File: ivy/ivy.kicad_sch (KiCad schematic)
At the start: 0 parts

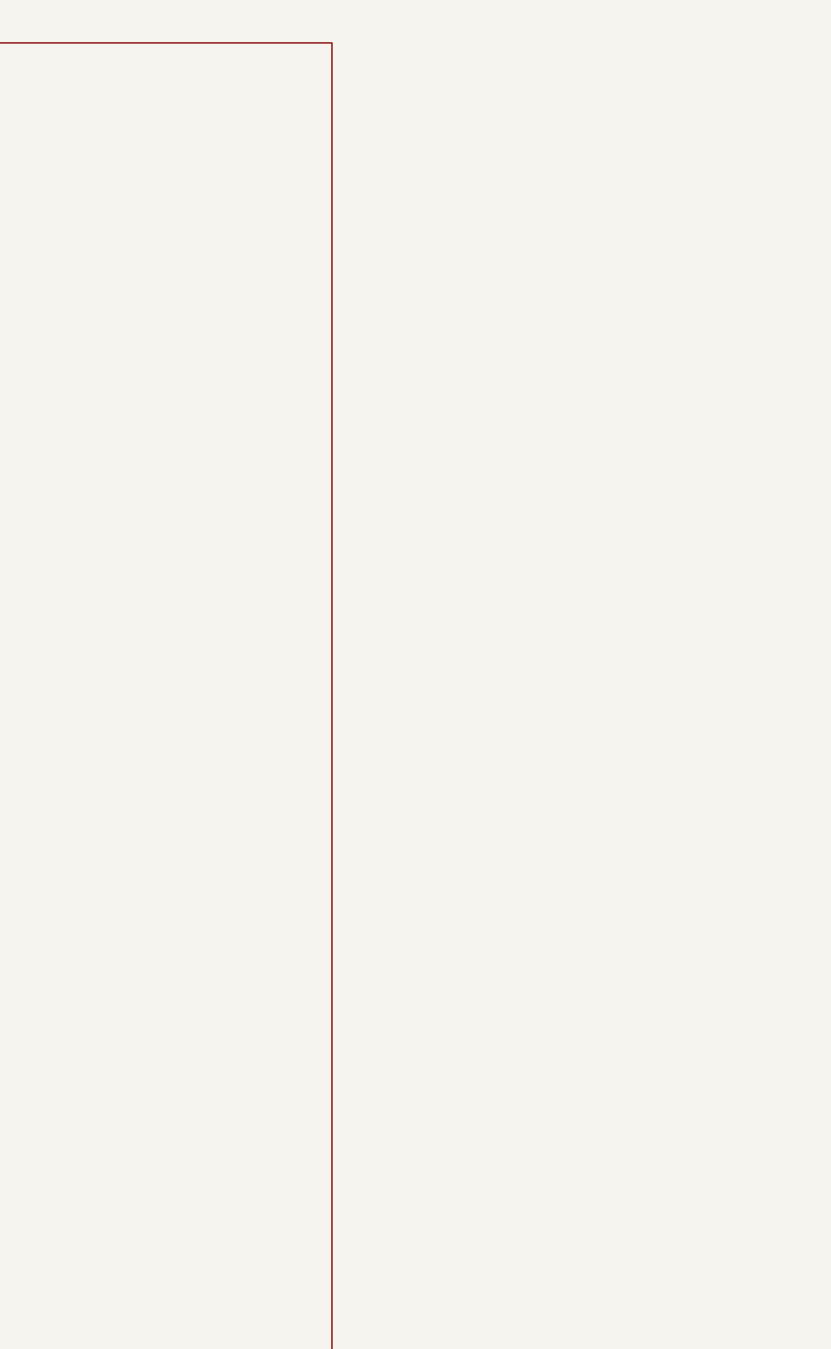
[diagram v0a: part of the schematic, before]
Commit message: create USB sheet
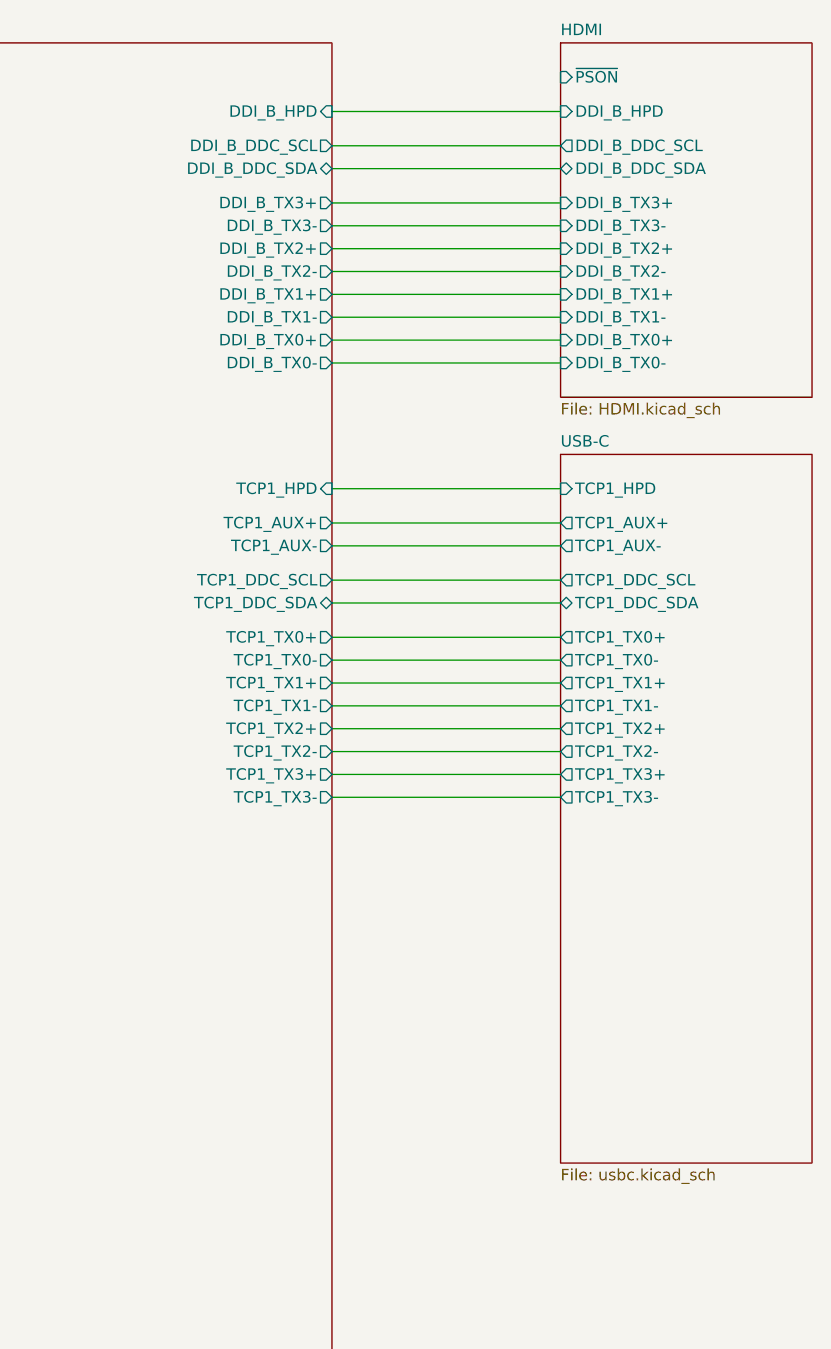
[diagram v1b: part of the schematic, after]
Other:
- added sheet HDMI (HDMI.kicad_sch)
- added sheet USB-C (usbc.kicad_sch)
- sheet LattePanda Module ports: added DDI_B_DDC_SCL, DDI_B_DDC_SDA, DDI_B_HPD, DDI_B_TX0+, DDI_B_TX0-, DDI_B_TX1+, DDI_B_TX1-, DDI_B_TX2+, DDI_B_TX2-, DDI_B_TX3+, DDI_B_TX3-, TCP1_AUX+, TCP1_AUX-, TCP1_DDC_SCL, TCP1_DDC_SDA, TCP1_HPD, TCP1_TX0+, TCP1_TX0-, TCP1_TX1+, TCP1_TX1-, TCP1_TX2+, TCP1_TX2-, TCP1_TX3+, TCP1_TX3-; removed none
